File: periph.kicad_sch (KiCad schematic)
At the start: 17 parts, among them U13 MQ-6, U14 BME680, U15 LSM6DS3

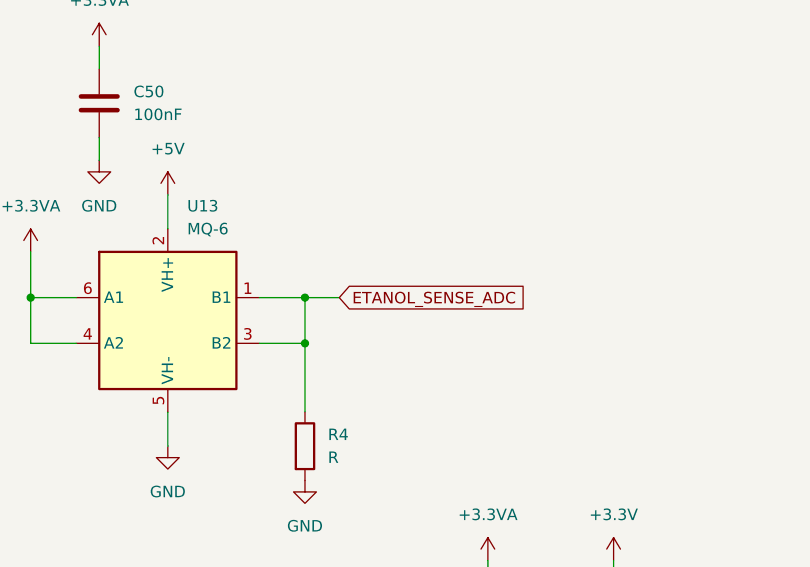
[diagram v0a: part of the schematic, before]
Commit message: test points and small fix
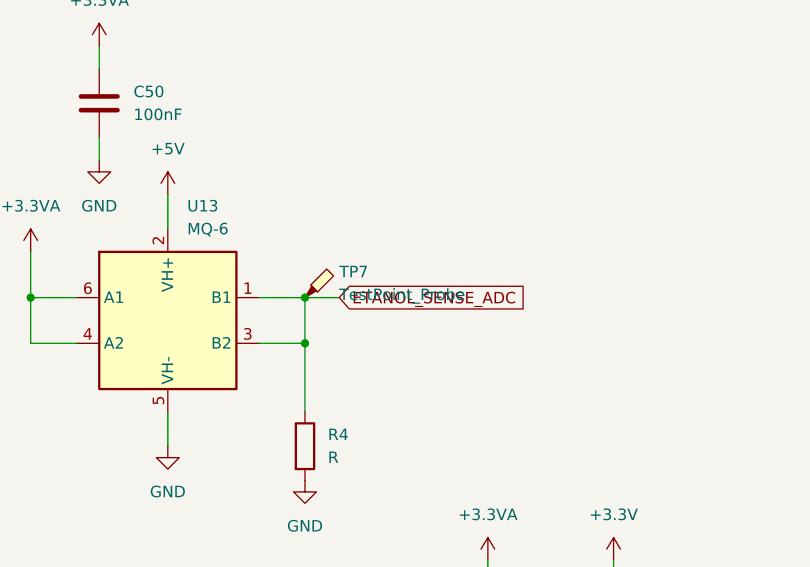
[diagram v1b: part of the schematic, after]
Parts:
- added TP7: TestPoint_Probe, symbol Connector:TestPoint_Probe
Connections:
- net ETANOL_SENSE_ADC: now also TP7.1
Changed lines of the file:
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@@
+	)
+	(symbol
+		(lib_id "Connector:TestPoint_Probe")
+		(at 194.31 59.69 0)
+		(unit 1)
+		(body_style 1)
+		(exclude_from_sim no)
+		(in_bom yes)
+		(on_board yes)
+		(in_pos_files yes)
+		(dnp no)
+		(fields_autoplaced yes)
+		(property "Reference" "TP7"
+			(at 198.12 56.8324 0)
+			(show_name no)
+			(do_not_autoplace no)
+			(effects
+				(font
+					(size 1.27 1.27)
+				)
+				(justify left)
+			)
+		)
+		(property "Value" "TestPoint_Probe"
+			(at 198.12 59.3724 0)
+			(show_name no)
+			(do_not_autoplace no)
+			(effects
+				(font
+					(size 1.27 1.27)
+				)
+				(justify left)
+			)
+		)
+		(property "Footprint" ""
+			(at 199.39 59.69 0)
+			(hide yes)
+			(show_name no)
+			(do_not_autoplace no)
+			(effects
+				(font
+					(size 1.27 1.27)
+				)
+			)
+		)
+		(property "Datasheet" ""
+			(at 199.39 59.69 0)
+			(hide yes)
+			(show_name no)
+			(do_not_autoplace no)
+			(effects
+				(font
+					(size 1.27 1.27)
+				)
+			)
+		)
+		(property "Description" "test point (alternative probe-style design)"
+			(at 194.31 59.69 0)
+			(hide yes)
+			(show_name no)
+			(do_not_autoplace no)
+			(effects
+				(font
+					(size 1.27 1.27)
+				)
+			)
+		)
+		(pin "1"
+		)
+		(instances
+			(project "iw18-hs"
+				(path "/9f21d1c7-829c-4910-99a9-b9bc821490d3/cc3711de-cfeb-4aec-8a45-cd304d109296"
+					(reference "TP7")
+					(unit 1)
+				)
+			)
+		)
 	)
 	(symbol

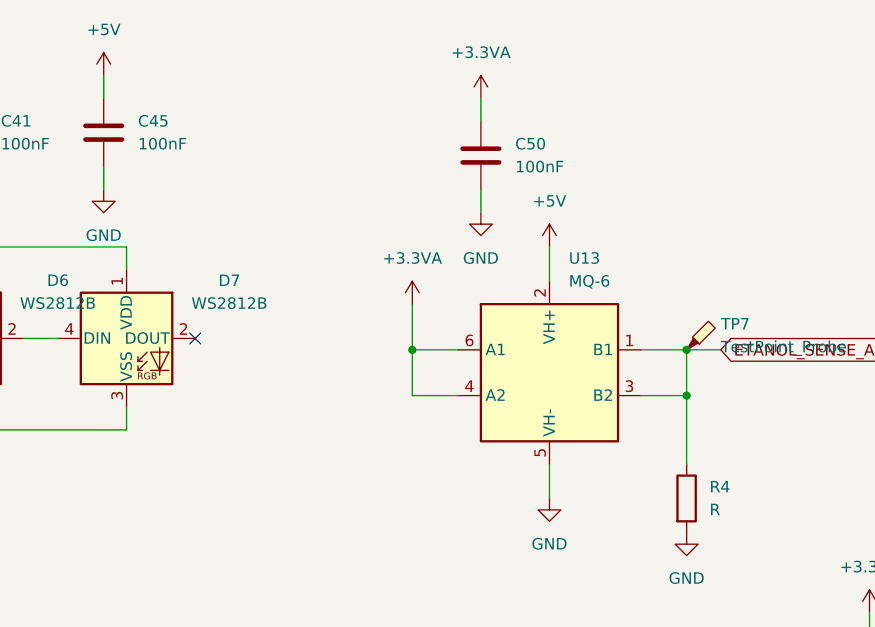
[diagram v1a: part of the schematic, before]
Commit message: sensor heat and some testpoints
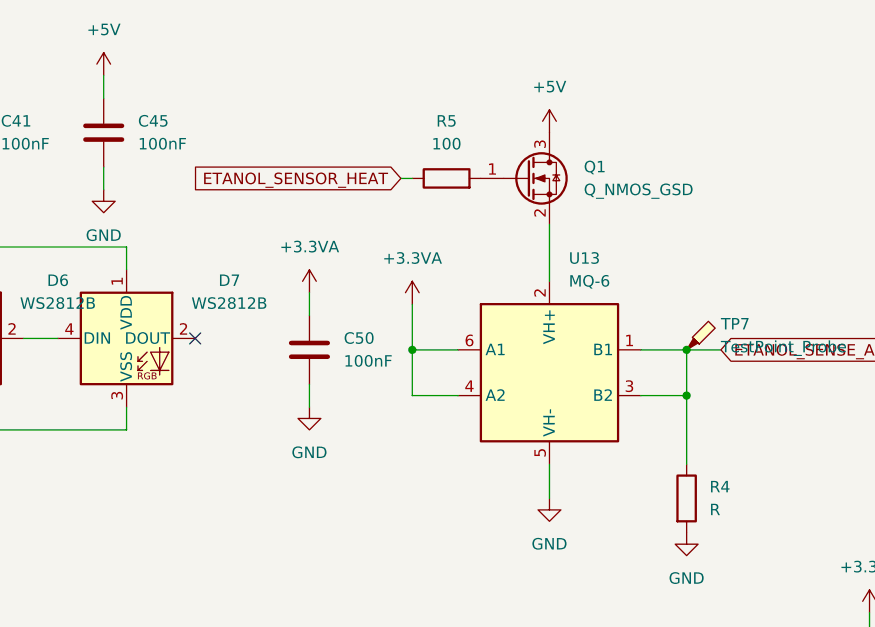
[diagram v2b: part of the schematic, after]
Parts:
- added Q1: Q_NMOS_GSD, Package_TO_SOT_SMD:SOT-23, symbol Transistor_FET:Q_NMOS_GSD
- added R5: 100, Resistor_SMD:R_0805_2012Metric, symbol Device:R
- TP7: footprint (none) -> TestPoint:TestPoint_THTPad_D2.0mm_Drill1.0mm
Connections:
- net +5V: now also Q1.3 (D); no longer U13.2 (VH+)
- new net: Q1.1 (G), R5.2
- new net: Q1.2 (S), U13.2 (VH+)
- new net ETANOL_SENSOR_HEAT: R5.1
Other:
- moved on the sheet: C50

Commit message: Do compoent placing
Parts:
- added J4, J5: Conn_02x08_Odd_Even, Connector_PinHeader_2.54mm:PinHeader_2x08_P2.54mm_Vertical, symbol Connector_Generic:Conn_02x08_Odd_Even
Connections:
- net +3.3V: now also J4.3 (Pin_3), J5.4 (Pin_4)
- net +3.3VA: now also J4.1 (Pin_1), J5.2 (Pin_2)
- net +5V: now also J4.5 (Pin_5), J4.7 (Pin_7), J5.6 (Pin_6), J5.8 (Pin_8)
- net ETANOL_SENSE_ADC: now also J4.12 (Pin_12), J5.11 (Pin_11)
- net ETANOL_SENSOR_HEAT: now also J4.14 (Pin_14), J5.13 (Pin_13)
- net GND: now also J4.11 (Pin_11), J4.13 (Pin_13), J4.15 (Pin_15), J4.16 (Pin_16), J4.2 (Pin_2), J4.9 (Pin_9), J5.1 (Pin_1), J5.10 (Pin_10), J5.12 (Pin_12), J5.14 (Pin_14), J5.15 (Pin_15), J5.16 (Pin_16)
- net IMU_INT0: now also J4.8 (Pin_8), J5.7 (Pin_7)
- net IMU_INT1: now also J4.10 (Pin_10), J5.9 (Pin_9)
- net SCL: now also J4.4 (Pin_4), J5.3 (Pin_3)
- net SDA: now also J4.6 (Pin_6), J5.5 (Pin_5)
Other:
- note added: "KURWA PANIE NMOS TUTEJ?"

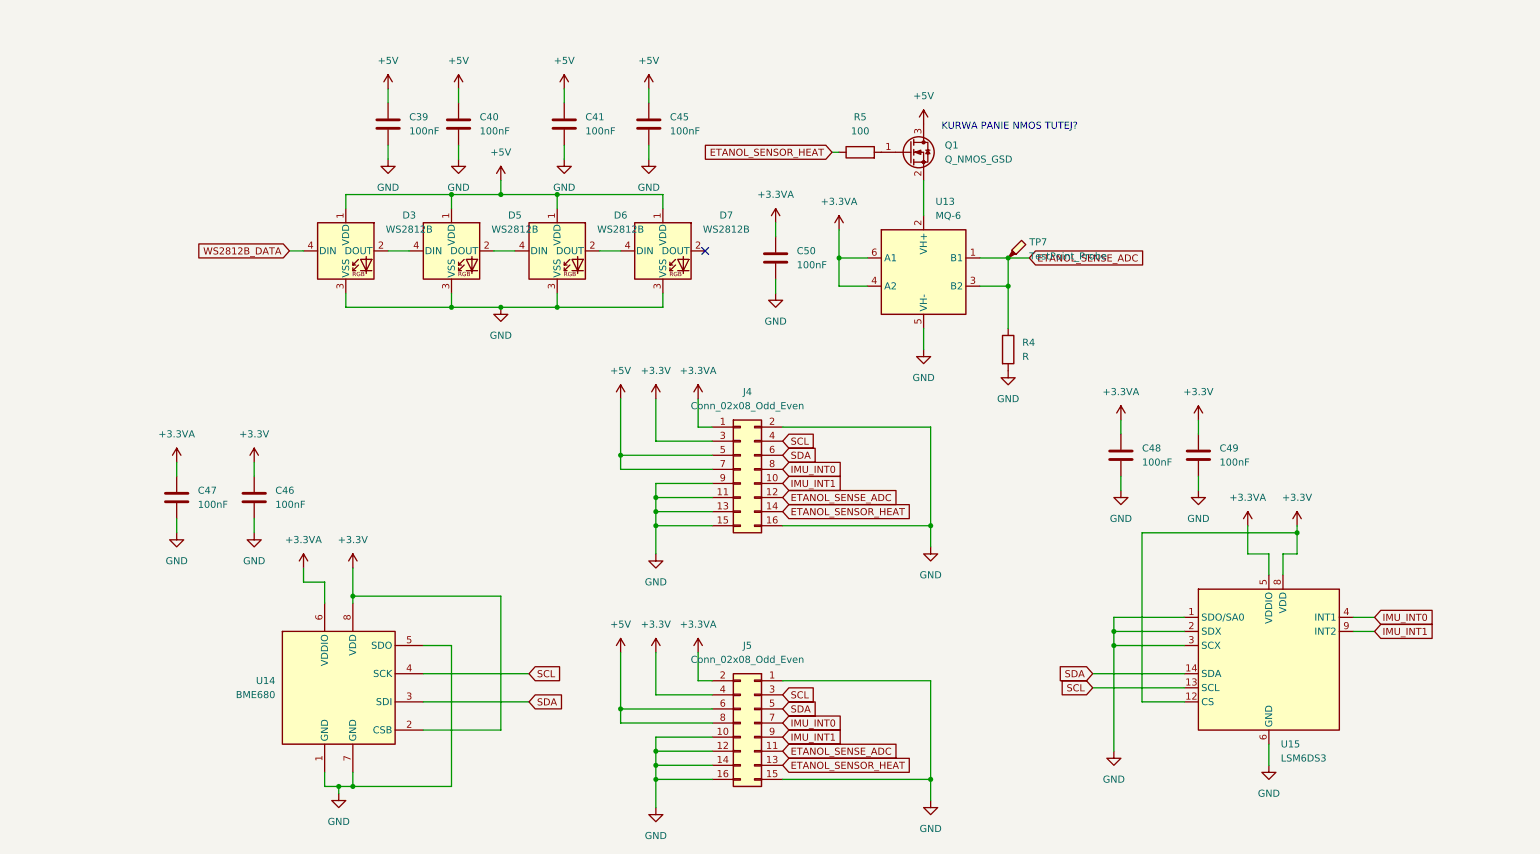
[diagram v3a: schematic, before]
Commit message: Refine board
* Add UART connector for chaining and controll
* shrink the board
workspace 1 output DP-6
* allow for pd controller eeprom programming
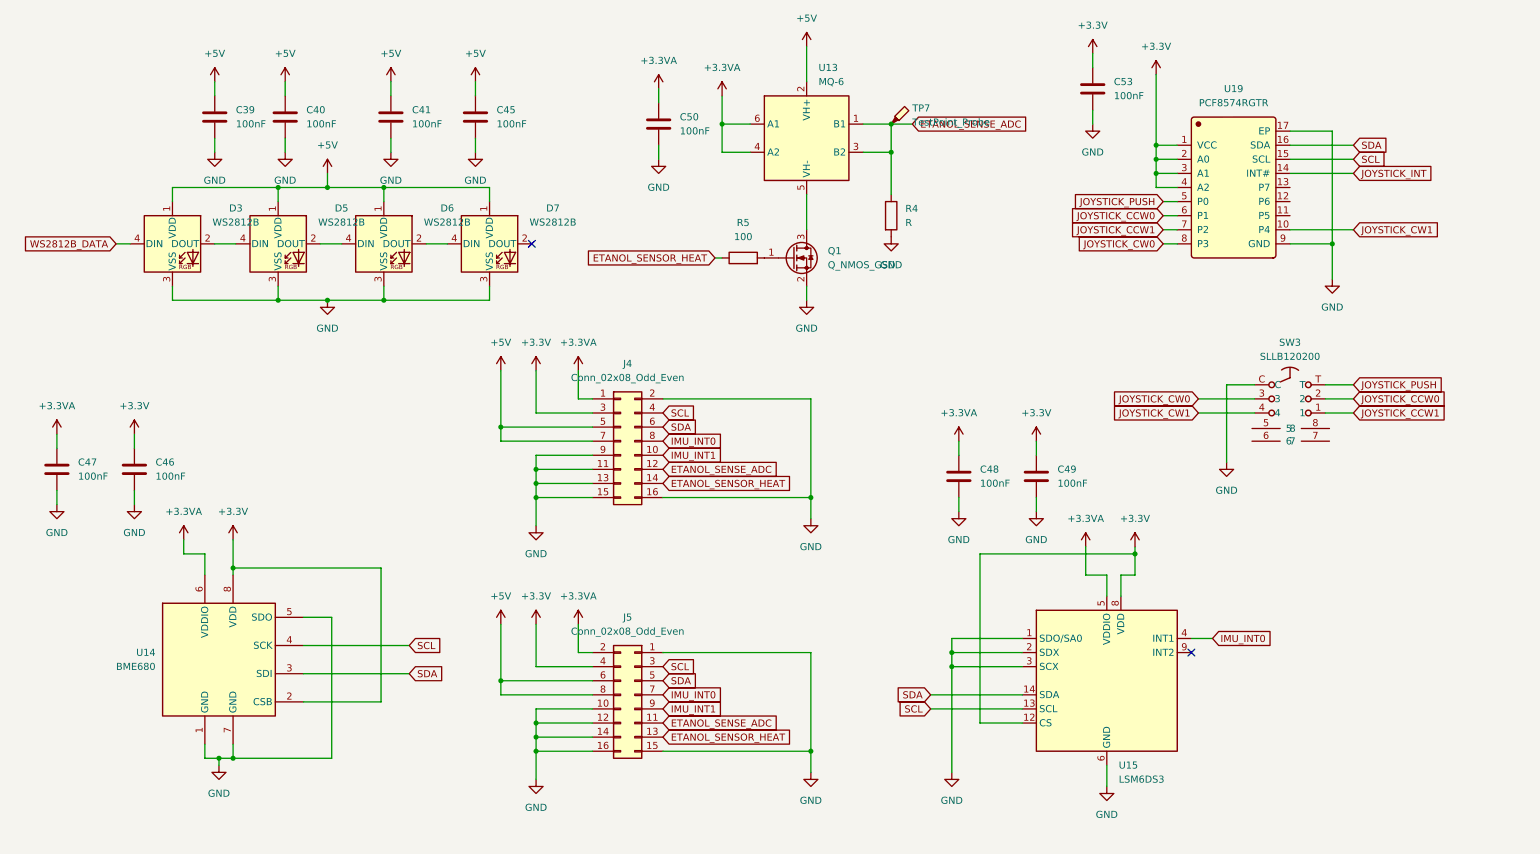
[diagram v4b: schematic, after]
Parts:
- added C53: 100nF, Capacitor_SMD:C_0805_2012Metric, symbol Device:C
- added SW3: SLLB120200, JLCImport:SLLB120200, symbol JLCImport:SLLB120200
- added U19: PCF8574RGTR, Package_DFN_QFN:WQFN-16-1EP_3x3mm_P0.5mm_EP1.6x1.6mm, symbol JLCImport:PCF8574RGTR
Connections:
- net +3.3V: now also C53.1, U19.1 (VCC), U19.2 (A0), U19.3 (A1), U19.4 (A2)
- net +5V: now also U13.2 (VH+); no longer Q1.3 (D)
- net GND: now also Q1.2 (S), C53.2, SW3.C, U19.17 (EP), U19.9 (GND); no longer U13.5 (VH-)
- net IMU_INT1: no longer U15.9 (INT2)
- net SCL: now also U19.15 (SCL)
- net SDA: now also U19.16 (SDA)
- new net: Q1.3 (D), U13.5 (VH-)
- new net JOYSTICK_CCW0: SW3.2, U19.6 (P1)
- new net JOYSTICK_CCW1: SW3.1, U19.7 (P2)
- new net JOYSTICK_CW0: SW3.3, U19.8 (P3)
- new net JOYSTICK_CW1: SW3.4, U19.10 (P4)
- new net JOYSTICK_INT: U19.14 (INT#)
- new net JOYSTICK_PUSH: SW3.T, U19.5 (P0)
- no-connect marks 1 -> 2
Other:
- note removed: "KURWA PANIE NMOS TUTEJ?"
- moved on the sheet: C39, C40, C41, C45, C46, C47, C48, C49, C50, D3, D5, D6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

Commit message: Start routing
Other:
- moved on the sheet: R4, TP7
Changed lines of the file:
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@@
 	(wire
 		(pts
-			(xy 173.228 48.26) (xy 173.228 40.64)
+			(xy 176.53 43.18) (xy 176.53 40.64)
 		)
 		(stroke
@@
 	(wire
 		(pts
+			(xy 176.53 40.64) (xy 173.228 40.64)
+		)
+		(stroke
+			(width 0)
+			(type default)
+		)
+	)
+	(wire
+		(pts
 			(xy 109.22 143.51) (xy 119.38 143.51)
 		)
@@
 	(wire
 		(pts
+			(xy 181.61 27.94) (xy 173.228 35.56)
+		)
+		(stroke
+			(width 0)
+			(type default)
+		)
+	)
+	(wire
+		(pts
 			(xy 45.72 110.49) (xy 45.72 113.03)
 		)
@@
 	(symbol
 		(lib_id "Connector:TestPoint_Probe")
-		(at 173.228 35.56 0)
+		(at 181.61 27.94 0)
 		(unit 1)
 		(body_style 1)
@@
 		(fields_autoplaced yes)
 		(property "Reference" "TP7"
-			(at 177.038 32.7024 0)
+			(at 185.42 25.0824 0)
 			(show_name no)
 			(do_not_autoplace no)
@@
 		)
 		(property "Value" "TestPoint_Probe"
-			(at 177.038 35.2424 0)
+			(at 185.42 27.6224 0)
 			(show_name no)
 			(do_not_autoplace no)
@@
 		)
 		(property "Footprint" "TestPoint:TestPoint_THTPad_D2.0mm_Drill1.0mm"
-			(at 178.308 35.56 0)
+			(at 186.69 27.94 0)
 			(hide yes)
 			(show_name no)
@@
 		)
 		(property "Datasheet" ""
-			(at 178.308 35.56 0)
+			(at 186.69 27.94 0)
 			(hide yes)
 			(show_name no)
@@
 		)
 		(property "Description" "test point (alternative probe-style design)"
-			(at 173.228 35.56 0)
+			(at 181.61 27.94 0)
 			(hide yes)
 			(show_name no)
@@
 	(symbol
 		(lib_id "power:GND")
-		(at 173.228 55.88 0)
+		(at 176.53 50.8 0)
 		(unit 1)
 		(body_style 1)
@@
 		(fields_autoplaced yes)
 		(property "Reference" "#PWR071"
-			(at 173.228 62.23 0)
+			(at 176.53 57.15 0)
 			(hide yes)
 			(show_name no)
@@
 		)
 		(property "Value" "GND"
-			(at 173.228 60.96 0)
+			(at 176.53 55.88 0)
 			(show_name no)
 			(do_not_autoplace no)
@@
 		)
 		(property "Footprint" ""
-			(at 173.228 55.88 0)
+			(at 176.53 50.8 0)
 			(hide yes)
 			(show_name no)
@@
 		)
 		(property "Datasheet" ""
-			(at 173.228 55.88 0)
+			(at 176.53 50.8 0)
 			(hide yes)
 			(show_name no)
@@
 		)
 		(property "Description" "Power symbol creates a global label with name \"GND\" , ground"
-			(at 173.228 55.88 0)
+			(at 176.53 50.8 0)
 			(hide yes)
 			(show_name no)
@@
 	(symbol
 		(lib_id "Device:R")
-		(at 173.228 52.07 0)
+		(at 176.53 46.99 0)
 		(unit 1)
 		(body_style 1)
@@
 		(fields_autoplaced yes)
 		(property "Reference" "R4"
-			(at 175.768 50.7999 0)
+			(at 179.07 45.7199 0)
 			(show_name no)
 			(do_not_autoplace no)
@@
 		)
 		(property "Value" "R"
-			(at 175.768 53.3399 0)
+			(at 179.07 48.2599 0)
 			(show_name no)
 			(do_not_autoplace no)
@@
 		)
 		(property "Footprint" "Resistor_SMD:R_0805_2012Metric"
-			(at 171.45 52.07 90)
+			(at 174.752 46.99 90)
 			(hide yes)
 			(show_name no)
@@
 		)
 		(property "Datasheet" ""
-			(at 173.228 52.07 0)
+			(at 176.53 46.99 0)
 			(hide yes)
 			(show_name no)
@@
 		)
 		(property "Description" "Resistor"
-			(at 173.228 52.07 0)
+			(at 176.53 46.99 0)
 			(hide yes)
 			(show_name no)

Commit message: Route some
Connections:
- net JOYSTICK_CCW1: now also U19.5 (P0); no longer U19.7 (P2)
- net JOYSTICK_PUSH: now also U19.7 (P2); no longer U19.5 (P0)
- net PROGRAM_PD_CONTROLLER: now reaches U19.12 (P6)
